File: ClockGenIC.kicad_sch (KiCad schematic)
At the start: 9 parts, among them J5 Conn_Coaxial, U1 ADF4351, U4 ADF4351BCPZ-RL7

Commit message: updated schematic
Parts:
- removed U4: ADF4351BCPZ-RL7, CP_32_7_ADI, symbol ADF4351BCPZ-RL7:ADF4351BCPZ-RL7
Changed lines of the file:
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@@
-	)
-	(symbol
-		(lib_id "ADF4351BCPZ-RL7:ADF4351BCPZ-RL7")
-		(at 176.53 59.69 0)
-		(unit 1)
-		(exclude_from_sim no)
-		(in_bom yes)
-		(on_board yes)
-		(dnp no)
-		(fields_autoplaced yes)
-		(property "Reference" "U4"
-			(at 201.93 49.53 0)
-			(effects
-				(font
-					(size 1.524 1.524)
-				)
-			)
-		)
-		(property "Value" "ADF4351BCPZ-RL7"
-			(at 201.93 52.07 0)
-			(effects
-				(font
-					(size 1.524 1.524)
-				)
-			)
-		)
-		(property "Footprint" "CP_32_7_ADI"
-			(at 176.53 59.69 0)
-			(effects
-				(font
-					(size 1.27 1.27)
-					(italic yes)
-				)
-				(hide yes)
-			)
-		)
-		(property "Datasheet" "https://www.analog.com/media/en/technical-documentation/data-sheets/ADF4351.pdf"
-			(at 176.53 59.69 0)
-			(effects
-				(font
-					(size 1.27 1.27)
-					(italic yes)
-				)
-				(hide yes)
-			)
-		)
-		(property "Description" ""
-			(at 176.53 59.69 0)
-			(effects
-				(font
-					(size 1.27 1.27)
-				)
-				(hide yes)
-			)
-		)
-		(pin "1"
-		)
-		(pin "14"
-		)
-		(pin "2"
-		)
-		(pin "4"
-		)
-		(pin "9"
-		)
-		(pin "10"
-		)
-		(pin "11"
-		)
-		(pin "3"
-		)
-		(pin "5"
-		)
-		(pin "12"
-		)
-		(pin "13"
-		)
-		(pin "7"
-		)
-		(pin "6"
-		)
-		(pin "8"
-		)
-		(pin "33"
-		)
-		(pin "32"
-		)
-		(pin "29"
-		)
-		(pin "15"
-		)
-		(pin "27"
-		)
-		(pin "26"
-		)
-		(pin "30"
-		)
-		(pin "24"
-		)
-		(pin "28"
-		)
-		(pin "16"
-		)
-		(pin "25"
-		)
-		(pin "22"
-		)
-		(pin "23"
-		)
-		(pin "21"
-		)
-		(pin "31"
-		)
-		(pin "20"
-		)
-		(pin "19"
-		)
-		(pin "17"
-		)
-		(pin "18"
-		)
-		(instances
-			(project ""
-				(path "/e1444a2d-a0c4-493c-a136-c624dc084e46/5eadf96c-4633-4d78-8a47-09b3347a9db0"
-					(reference "U4")
-					(unit 1)
-				)
-			)
-		)
 	)
 	(symbol

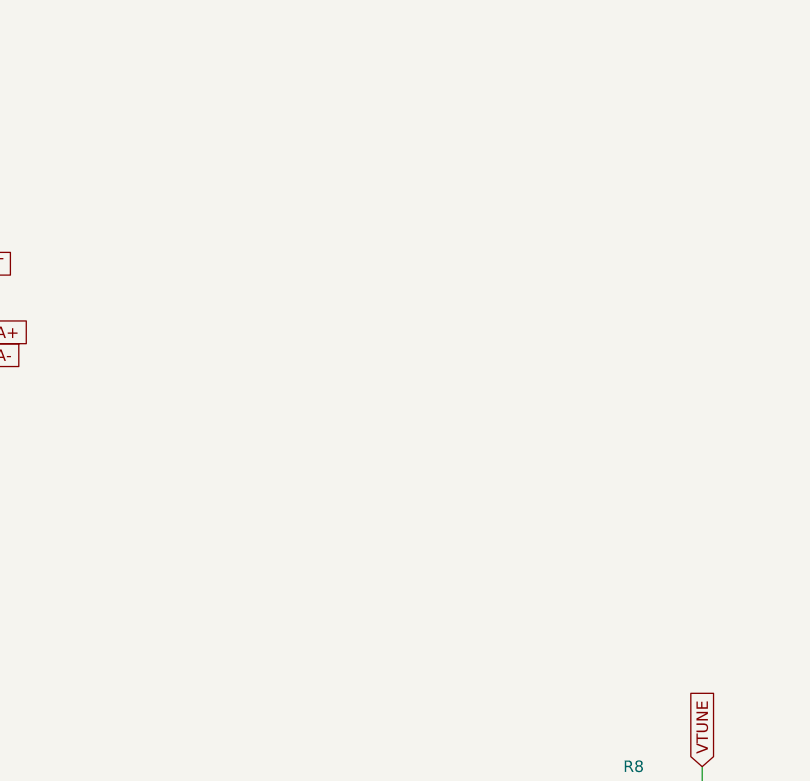
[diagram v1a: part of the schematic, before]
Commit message: Refact: Added other Clock gen IC footprint
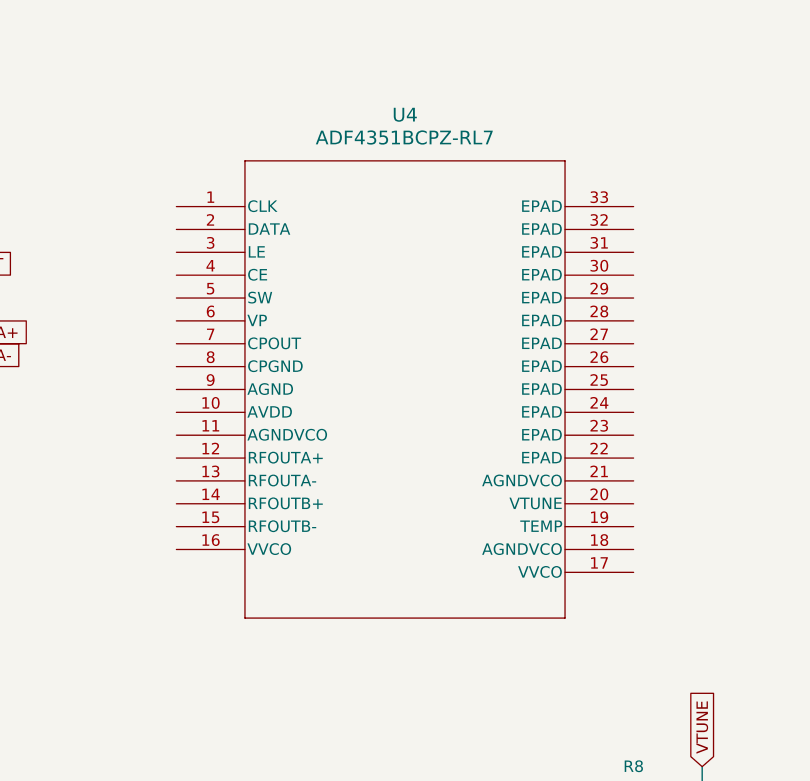
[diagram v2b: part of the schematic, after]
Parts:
- added U4: ADF4351BCPZ-RL7, CP_32_7_ADI, symbol ADF4351BCPZ-RL7:ADF4351BCPZ-RL7
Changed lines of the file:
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@@
+	)
+	(symbol
+		(lib_id "ADF4351BCPZ-RL7:ADF4351BCPZ-RL7")
+		(at 176.53 59.69 0)
+		(unit 1)
+		(exclude_from_sim no)
+		(in_bom yes)
+		(on_board yes)
+		(dnp no)
+		(fields_autoplaced yes)
+		(property "Reference" "U4"
+			(at 201.93 49.53 0)
+			(effects
+				(font
+					(size 1.524 1.524)
+				)
+			)
+		)
+		(property "Value" "ADF4351BCPZ-RL7"
+			(at 201.93 52.07 0)
+			(effects
+				(font
+					(size 1.524 1.524)
+				)
+			)
+		)
+		(property "Footprint" "CP_32_7_ADI"
+			(at 176.53 59.69 0)
+			(effects
+				(font
+					(size 1.27 1.27)
+					(italic yes)
+				)
+				(hide yes)
+			)
+		)
+		(property "Datasheet" "https://www.analog.com/media/en/technical-documentation/data-sheets/ADF4351.pdf"
+			(at 176.53 59.69 0)
+			(effects
+				(font
+					(size 1.27 1.27)
+					(italic yes)
+				)
+				(hide yes)
+			)
+		)
+		(property "Description" ""
+			(at 176.53 59.69 0)
+			(effects
+				(font
+					(size 1.27 1.27)
+				)
+				(hide yes)
+			)
+		)
+		(pin "1"
+		)
+		(pin "14"
+		)
+		(pin "2"
+		)
+		(pin "4"
+		)
+		(pin "9"
+		)
+		(pin "10"
+		)
+		(pin "11"
+		)
+		(pin "3"
+		)
+		(pin "5"
+		)
+		(pin "12"
+		)
+		(pin "13"
+		)
+		(pin "7"
+		)
+		(pin "6"
+		)
+		(pin "8"
+		)
+		(pin "33"
+		)
+		(pin "32"
+		)
+		(pin "29"
+		)
+		(pin "15"
+		)
+		(pin "27"
+		)
+		(pin "26"
+		)
+		(pin "30"
+		)
+		(pin "24"
+		)
+		(pin "28"
+		)
+		(pin "16"
+		)
+		(pin "25"
+		)
+		(pin "22"
+		)
+		(pin "23"
+		)
+		(pin "21"
+		)
+		(pin "31"
+		)
+		(pin "20"
+		)
+		(pin "19"
+		)
+		(pin "17"
+		)
+		(pin "18"
+		)
+		(instances
+			(project ""
+				(path "/e1444a2d-a0c4-493c-a136-c624dc084e46/5eadf96c-4633-4d78-8a47-09b3347a9db0"
+					(reference "U4")
+					(unit 1)
+				)
+			)
+		)
 	)
 	(symbol
